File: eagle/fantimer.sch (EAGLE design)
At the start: 16 parts, among them IC1 PIC10F200, K1 PB2032-ND, Q1 2N7000-G, U1 IRM-01-5, X1 732-10957-ND

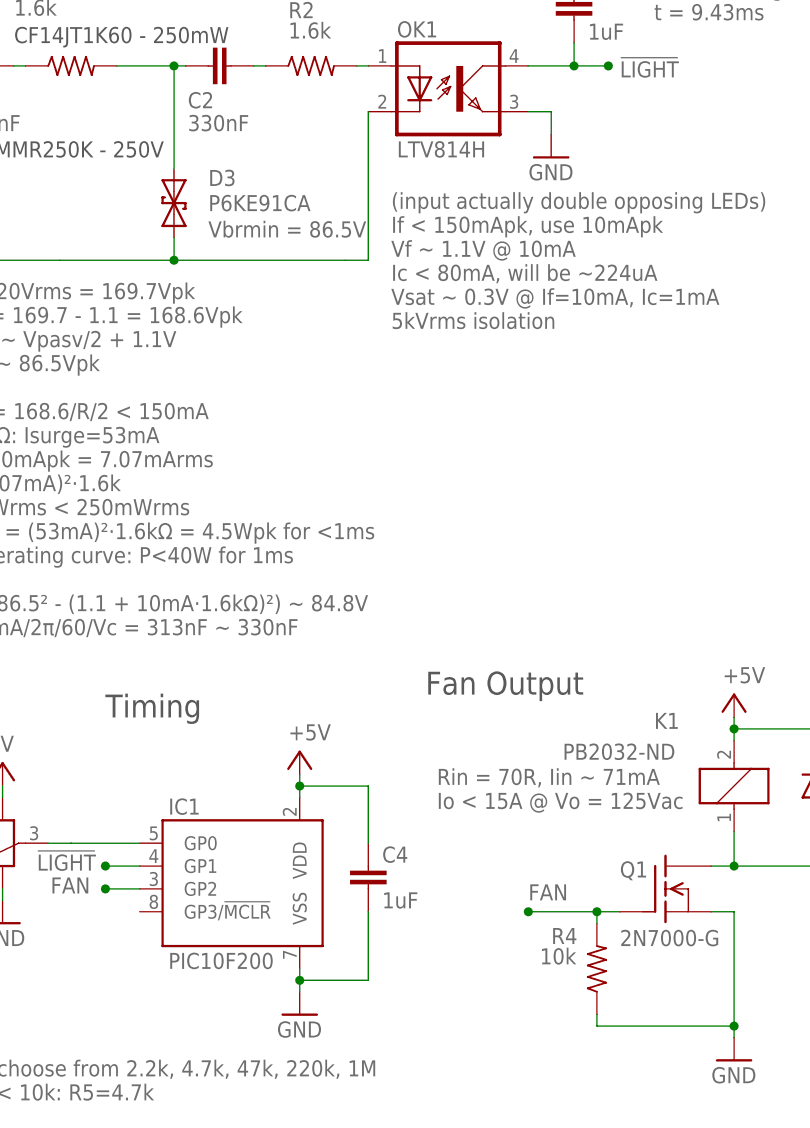
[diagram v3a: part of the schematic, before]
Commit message: Pulldown 100k. Fix up diodes, resistors and filter cap in BOM.
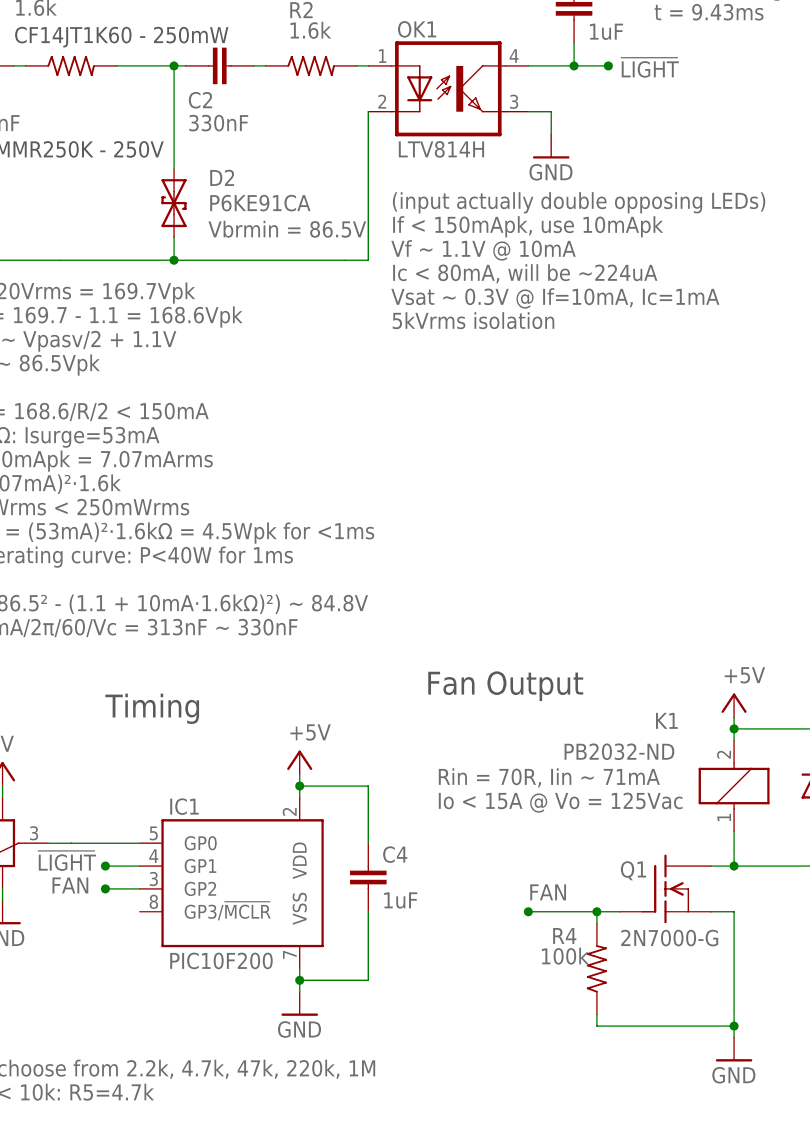
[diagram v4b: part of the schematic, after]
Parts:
- R4: value 10k -> 100k
- renumbered D3 to D2
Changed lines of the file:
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@@
 <part name="P+4" library="supply1" library_urn="urn:adsk.eagle:library:371" deviceset="+5V" device=""/>
 <part name="GND4" library="supply1" library_urn="urn:adsk.eagle:library:371" deviceset="GND" device=""/>
-<part name="D3" library="diode" library_urn="urn:adsk.eagle:library:210" deviceset="P6KEXXC" device="" package3d_urn="urn:adsk.eagle:package:43349/1" value="P6KE91CA"/>
+<part name="D2" library="diode" library_urn="urn:adsk.eagle:library:210" deviceset="P6KEXXC" device="" package3d_urn="urn:adsk.eagle:package:43349/1" value="P6KE91CA"/>
 <part name="C1" library="rcl" library_urn="urn:adsk.eagle:library:334" deviceset="C-EU" device="102-064X133" package3d_urn="urn:adsk.eagle:package:23653/1" value="330nF"/>
 <part name="C2" library="rcl" library_urn="urn:adsk.eagle:library:334" deviceset="C-EU" device="102-064X133" package3d_urn="urn:adsk.eagle:package:23653/1" value="330nF"/>
@@
 <part name="IC1" library="microchip-addl" deviceset="PIC10F220" device="-I/P" package3d_urn="urn:adsk.eagle:package:14440/1" value="PIC10F200"/>
 <part name="GND2" library="supply1" library_urn="urn:adsk.eagle:library:371" deviceset="GND" device=""/>
-<part name="R4" library="resistor" library_urn="urn:adsk.eagle:library:348" deviceset="R-US_" device="0207/7" package3d_urn="urn:adsk.eagle:package:25942/1" value="10k"/>
+<part name="R4" library="resistor" library_urn="urn:adsk.eagle:library:348" deviceset="R-US_" device="0207/7" package3d_urn="urn:adsk.eagle:package:25942/1" value="100k"/>
 <part name="C4" library="rcl" library_urn="urn:adsk.eagle:library:334" deviceset="C-EU" device="025-025X050" package3d_urn="urn:adsk.eagle:package:23629/2" value="1uF"/>
 </parts>
@@
 </instance>
 <instance part="GND4" gate="1" x="77.47" y="121.92"/>
-<instance part="D3" gate="1" x="35.56" y="115.57" smashed="yes" rot="R90">
+<instance part="D2" gate="1" x="35.56" y="115.57" smashed="yes" rot="R90">
 <attribute name="NAME" x="39.37" y="118.745" size="1.778" layer="95"/>
 <attribute name="VALUE" x="39.37" y="115.951" size="1.778" layer="96"/>
@@
 <pinref part="OK1" gate="G$1" pin="C"/>
 <wire x1="57.15" y1="125.73" x2="57.15" y2="127" width="0.1524" layer="91"/>
-<pinref part="D3" gate="1" pin="1"/>
+<pinref part="D2" gate="1" pin="1"/>
 <wire x1="35.56" y1="113.03" x2="35.56" y2="110.49" width="0.1524" layer="91"/>
 <junction x="35.56" y="110.49"/>
@@
 <net name="VZ" class="0">
 <segment>
-<pinref part="D3" gate="1" pin="2"/>
+<pinref part="D2" gate="1" pin="2"/>
 <wire x1="35.56" y1="120.65" x2="35.56" y2="132.08" width="0.1524" layer="91"/>
 <pinref part="C2" gate="G$1" pin="1"/>

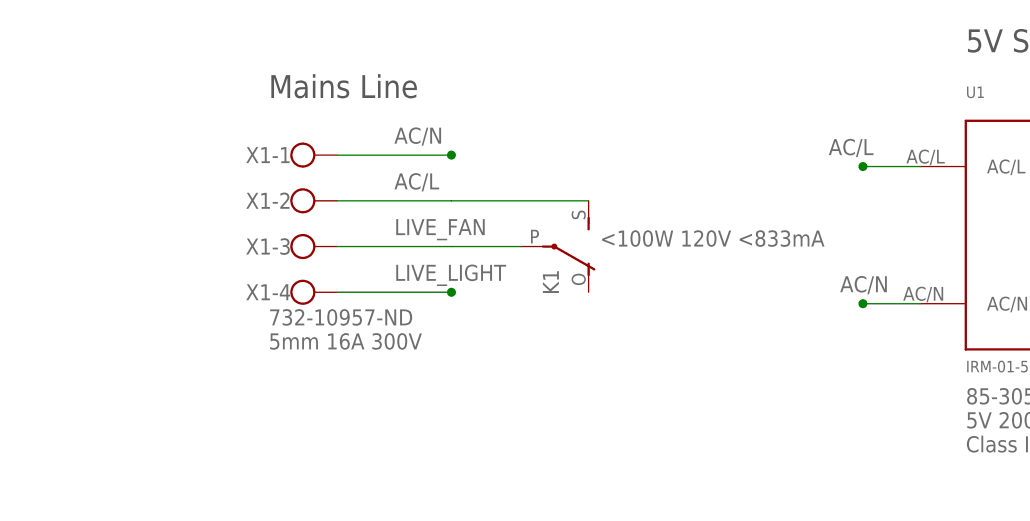
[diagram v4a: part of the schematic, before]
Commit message: Replace TVS with varistor across relay
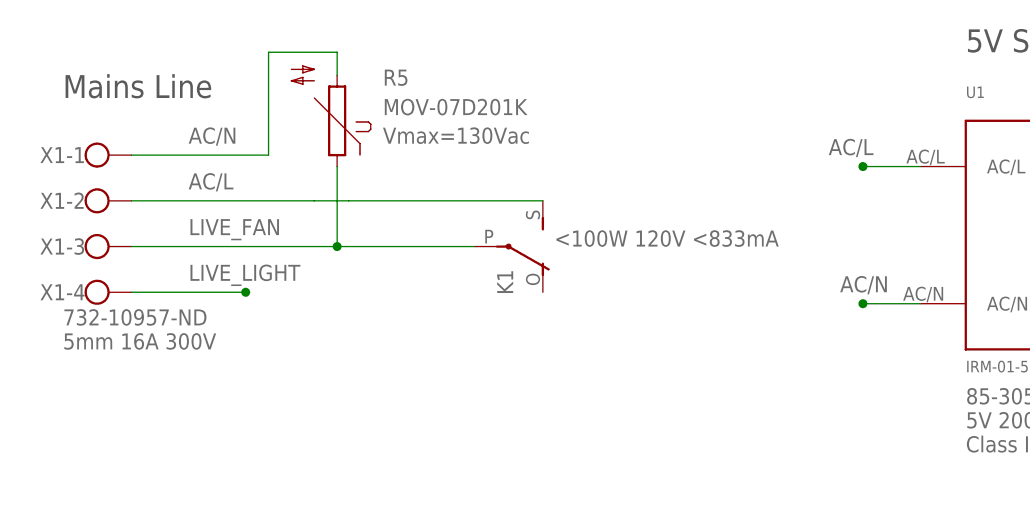
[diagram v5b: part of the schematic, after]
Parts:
- added R5: MOV-07D201K, varistor:S05K300
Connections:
- net AC/N: now also R5.2
- net LIVE_FAN: now also R5.1
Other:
- note added: "Vmax=130Vac"
- moved on the sheet: K1, X1-1, X1-2, X1-3, X1-4
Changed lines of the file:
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@@
 <part name="R4" library="resistor" library_urn="urn:adsk.eagle:library:348" deviceset="R-US_" device="0207/7" package3d_urn="urn:adsk.eagle:package:25942/1" value="100k"/>
 <part name="C4" library="rcl" library_urn="urn:adsk.eagle:library:334" deviceset="C-EU" device="025-025X050" package3d_urn="urn:adsk.eagle:package:23629/2" value="1uF"/>
+<part name="R5" library="varistor" library_urn="urn:adsk.eagle:library:410" deviceset="S05K300" device="" package3d_urn="urn:adsk.eagle:package:30536/1" value="MOV-07D201K"/>
 </parts>
 <sheets>
 <sheet>
 <plain>
-<text x="8.89" y="172.72" size="1.778" layer="96">5mm 16A 300V</text>
+<text x="-13.97" y="172.72" size="1.778" layer="96">5mm 16A 300V</text>
 <text x="7.62" y="21.59" size="1.778" layer="96" rot="MR180">R3 can choose from 2.2k, 4.7k, 47k, 220k, 1M
 Rinadc &lt; 10k: R5=4.7k</text>
@@
 5V 200mA out
 Class II isolation</text>
-<text x="45.72" y="184.15" size="1.778" layer="96">&lt;100W 120V &lt;833mA</text>
+<text x="40.64" y="184.15" size="1.778" layer="96">&lt;100W 120V &lt;833mA</text>
 <text x="64.77" y="49.53" size="1.778" layer="96">Rin = 70R, Iin ~ 71mA
 Io &lt; 15A @ Vo = 125Vac</text>
@@
 <text x="17.78" y="134.62" size="1.778" layer="97">CF14JT1K60‎ - 250mW</text>
 <text x="11.43" y="121.92" size="1.778" layer="97">334MMR250K‎ - 250V</text>
-<text x="8.89" y="200.66" size="2.54" layer="97">Mains Line</text>
+<text x="-13.97" y="200.66" size="2.54" layer="97">Mains Line</text>
 <text x="86.36" y="205.74" size="2.54" layer="97">5V Supply</text>
 <text x="11.43" y="147.32" size="2.54" layer="97">Line Detection</text>
 <text x="63.5" y="62.23" size="2.54" layer="97">Fan Output</text>
 <text x="27.94" y="59.69" size="2.54" layer="97">Timing</text>
+<text x="21.59" y="195.58" size="1.778" layer="96">Vmax=130Vac</text>
 </plain>
 <instances>
-<instance part="X1" gate="-1" x="11.43" y="194.31"/>
-<instance part="X1" gate="-2" x="11.43" y="189.23"/>
-<instance part="X1" gate="-3" x="11.43" y="184.15"/>
-<instance part="X1" gate="-4" x="11.43" y="179.07"/>
+<instance part="X1" gate="-1" x="-11.43" y="194.31"/>
+<instance part="X1" gate="-2" x="-11.43" y="189.23"/>
+<instance part="X1" gate="-3" x="-11.43" y="184.15"/>
+<instance part="X1" gate="-4" x="-11.43" y="179.07"/>
 <instance part="P+1" gate="1" x="120.65" y="200.66" smashed="yes">
 <attribute name="VALUE" x="119.38" y="201.93" size="1.778" layer="96"/>
@@
 <attribute name="PART" x="88.9" y="58.42" size="1.778" layer="95"/>
 </instance>
-<instance part="K1" gate="2" x="39.37" y="184.15" rot="R270"/>
+<instance part="K1" gate="2" x="34.29" y="184.15" rot="R270"/>
 <instance part="P+3" gate="1" x="97.79" y="62.23" smashed="yes">
 <attribute name="VALUE" x="96.52" y="63.5" size="1.778" layer="96"/>
@@
 </instance>
 <instance part="C4" gate="G$1" x="57.15" y="43.18"/>
+<instance part="R5" gate="G$1" x="16.51" y="198.12" smashed="yes" rot="R90">
+<attribute name="NAME" x="21.59" y="202.0316" size="1.778" layer="95"/>
+<attribute name="VALUE" x="21.59" y="198.755" size="1.778" layer="96"/>
+</instance>
 </instances>
 <busses>
@@
 <segment>
 <pinref part="X1" gate="-1" pin="KL"/>
-<wire x1="16.51" y1="194.31" x2="29.21" y2="194.31" width="0.1524" layer="91"/>
-<junction x="29.21" y="194.31"/>
-<label x="22.86" y="195.58" size="1.778" layer="95"/>
+<wire x1="-6.35" y1="194.31" x2="8.89" y2="194.31" width="0.1524" layer="91"/>
+<label x="0" y="195.58" size="1.778" layer="95"/>
+<wire x1="16.51" y1="203.2" x2="16.51" y2="205.74" width="0.1524" layer="91"/>
+<wire x1="16.51" y1="205.74" x2="8.89" y2="205.74" width="0.1524" layer="91"/>
+<wire x1="8.89" y1="205.74" x2="8.89" y2="194.31" width="0.1524" layer="91"/>
+<pinref part="R5" gate="G$1" pin="2"/>
 </segment>
 <segment>
@@
 <segment>
 <pinref part="X1" gate="-2" pin="KL"/>
-<wire x1="16.51" y1="189.23" x2="29.21" y2="189.23" width="0.1524" layer="91"/>
-<label x="22.86" y="190.5" size="1.778" layer="95"/>
+<wire x1="-6.35" y1="189.23" x2="13.97" y2="189.23" width="0.1524" layer="91"/>
+<wire x1="13.97" y1="189.23" x2="16.51" y2="189.23" width="0.1524" layer="91"/>
+<wire x1="16.51" y1="189.23" x2="17.78" y2="189.23" width="0.1524" layer="91"/>
+<label x="0" y="190.5" size="1.778" layer="95"/>
 <pinref part="K1" gate="2" pin="S"/>
-<wire x1="29.21" y1="189.23" x2="44.45" y2="189.23" width="0.1524" layer="91"/>
+<wire x1="17.78" y1="189.23" x2="39.37" y2="189.23" width="0.1524" layer="91"/>
 </segment>
 <segment>
@@
 <segment>
 <pinref part="X1" gate="-3" pin="KL"/>
-<wire x1="16.51" y1="184.15" x2="29.21" y2="184.15" width="0.1524" layer="91"/>
-<label x="22.86" y="185.42" size="1.778" layer="95"/>
+<wire x1="-6.35" y1="184.15" x2="16.51" y2="184.15" width="0.1524" layer="91"/>
+<label x="0" y="185.42" size="1.778" layer="95"/>
 <pinref part="K1" gate="2" pin="P"/>
-<wire x1="29.21" y1="184.15" x2="36.83" y2="184.15" width="0.1524" layer="91"/>
+<wire x1="16.51" y1="184.15" x2="31.75" y2="184.15" width="0.1524" layer="91"/>
+<wire x1="16.51" y1="193.04" x2="16.51" y2="184.15" width="0.1524" layer="91"/>
+<junction x="16.51" y="184.15"/>
+<pinref part="R5" gate="G$1" pin="1"/>
 </segment>
 </net>
@@
 <segment>
 <pinref part="X1" gate="-4" pin="KL"/>
-<wire x1="16.51" y1="179.07" x2="29.21" y2="179.07" width="0.1524" layer="91"/>
-<junction x="29.21" y="179.07"/>
-<label x="22.86" y="180.34" size="1.778" layer="95"/>
+<wire x1="-6.35" y1="179.07" x2="6.35" y2="179.07" width="0.1524" layer="91"/>
+<junction x="6.35" y="179.07"/>
+<label x="0" y="180.34" size="1.778" layer="95"/>
 </segment>
 <segment>

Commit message: Library updates
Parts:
- IC1: value PIC10F200 -> PIC10F220
- U1: device meanwell:IRM-01 -> meanwell:IRM-01-5
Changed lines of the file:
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@@
 <part name="P+3" library="supply1" library_urn="urn:adsk.eagle:library:371" deviceset="+5V" device=""/>
 <part name="D1" library="diode" library_urn="urn:adsk.eagle:library:210" deviceset="DIODE-" device="DO41-7.6" package3d_urn="urn:adsk.eagle:package:43421/1" value="SB140TA"/>
-<part name="U1" library="meanwell" deviceset="IRM-01" device="" value="IRM-01-5"/>
+<part name="U1" library="meanwell" deviceset="IRM-01-5" device="" value="IRM-01-5"/>
 <part name="OK1" library="optocoupler" library_urn="urn:adsk.eagle:library:320" deviceset="LTV816" device="" package3d_urn="urn:adsk.eagle:package:21938/1" value="LTV814H"/>
-<part name="R2" library="resistor" library_urn="urn:adsk.eagle:library:348" deviceset="R-US_" device="0207/7" package3d_urn="urn:adsk.eagle:package:25942/1" value="1.6k"/>
+<part name="R2" library="resistor" library_urn="urn:adsk.eagle:library:348" deviceset="R-US_" device="0207/7" package3d_urn="urn:adsk.eagle:package:23493/1" value="1.6k"/>
 <part name="P+4" library="supply1" library_urn="urn:adsk.eagle:library:371" deviceset="+5V" device=""/>
 <part name="GND4" library="supply1" library_urn="urn:adsk.eagle:library:371" deviceset="GND" device=""/>
@@
 <part name="C1" library="rcl" library_urn="urn:adsk.eagle:library:334" deviceset="C-EU" device="102-064X133" package3d_urn="urn:adsk.eagle:package:23653/1" value="330nF"/>
 <part name="C2" library="rcl" library_urn="urn:adsk.eagle:library:334" deviceset="C-EU" device="102-064X133" package3d_urn="urn:adsk.eagle:package:23653/1" value="330nF"/>
-<part name="R1" library="resistor" library_urn="urn:adsk.eagle:library:348" deviceset="R-US_" device="0207/7" package3d_urn="urn:adsk.eagle:package:25942/1" value="1.6k"/>
+<part name="R1" library="resistor" library_urn="urn:adsk.eagle:library:348" deviceset="R-US_" device="0207/7" package3d_urn="urn:adsk.eagle:package:23493/1" value="1.6k"/>
 <part name="R3" library="rcl" library_urn="urn:adsk.eagle:library:334" deviceset="POTENTIOMETER_" device="PT-10" package3d_urn="urn:adsk.eagle:package:23786/1" value="4.7k"/>
 <part name="P+6" library="supply1" library_urn="urn:adsk.eagle:library:371" deviceset="+5V" device=""/>
@@
 <part name="C3" library="rcl" library_urn="urn:adsk.eagle:library:334" deviceset="C-EU" device="025-025X050" package3d_urn="urn:adsk.eagle:package:23629/2" value="1uF"/>
 <part name="P+2" library="supply1" library_urn="urn:adsk.eagle:library:371" deviceset="+5V" device=""/>
-<part name="IC1" library="microchip-addl" deviceset="PIC10F220" device="-I/P" package3d_urn="urn:adsk.eagle:package:14440/1" value="PIC10F200"/>
+<part name="IC1" library="microchip-addl" deviceset="PIC10F220" device="-I/P" package3d_urn="urn:adsk.eagle:package:14440/1" value="PIC10F220"/>
 <part name="GND2" library="supply1" library_urn="urn:adsk.eagle:library:371" deviceset="GND" device=""/>
-<part name="R4" library="resistor" library_urn="urn:adsk.eagle:library:348" deviceset="R-US_" device="0207/7" package3d_urn="urn:adsk.eagle:package:25942/1" value="100k"/>
+<part name="R4" library="resistor" library_urn="urn:adsk.eagle:library:348" deviceset="R-US_" device="0207/7" package3d_urn="urn:adsk.eagle:package:23493/1" value="100k"/>
 <part name="C4" library="rcl" library_urn="urn:adsk.eagle:library:334" deviceset="C-EU" device="025-025X050" package3d_urn="urn:adsk.eagle:package:23629/2" value="1uF"/>
 <part name="R5" library="varistor" library_urn="urn:adsk.eagle:library:410" deviceset="S05K300" device="" package3d_urn="urn:adsk.eagle:package:30536/1" value="MOV-07D201K"/>
@@
 <attribute name="VALUE" x="17.78" y="55.88" size="1.778" layer="96" rot="MR0"/>
 </instance>
-<instance part="IC1" gate="G$1" x="46.99" y="44.45"/>
+<instance part="IC1" gate="G$1" x="43.18" y="41.91"/>
 <instance part="GND2" gate="1" x="49.53" y="26.67"/>
 <instance part="R4" gate="G$1" x="82.55" y="31.75" smashed="yes" rot="R90">

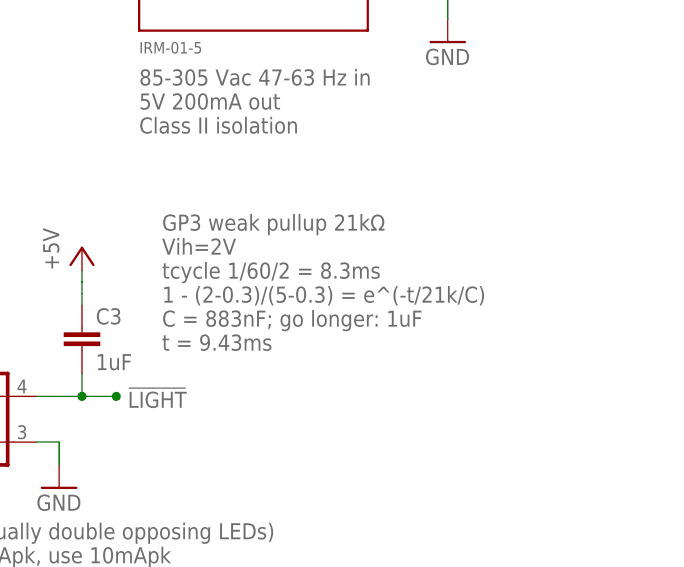
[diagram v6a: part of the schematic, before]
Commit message: Fix pullup info
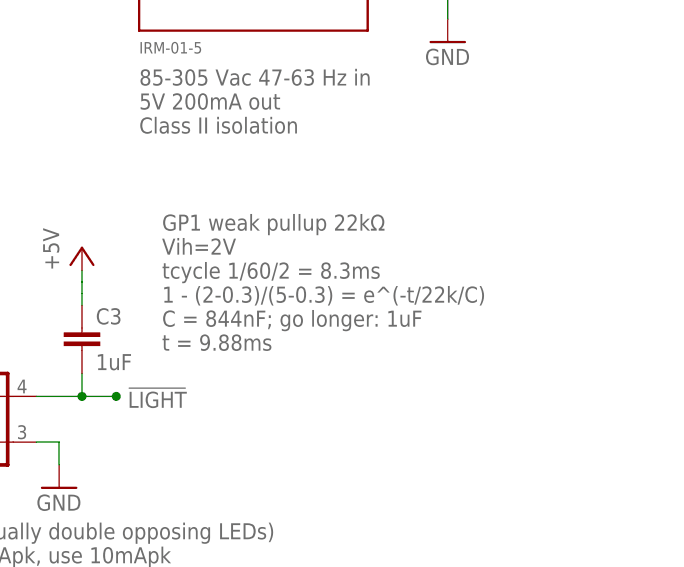
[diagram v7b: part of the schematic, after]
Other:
- note added: "GP1 weak pullup 22kΩ Vih=2V tcycle 1/60/2 = 8.3ms 1 - (2-0.3)/(5-0.3) = e^(-t/22k/C) C = 844nF; go longer: 1uF t = 9.88ms"
- note removed: "GP3 weak pullup 21kΩ Vih=2V tcycle 1/60/2 = 8.3ms 1 - (2-0.3)/(5-0.3) = e^(-t/21k/C) C = 883nF; go longer: 1uF t = 9.43ms"
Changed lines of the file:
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@@
 C = 10mA/2π/60/Vc = 313nF ~ 330nF</text>
 <text x="39.37" y="113.03" size="1.778" layer="96">Vbrmin = 86.5V</text>
-<text x="88.9" y="137.16" size="1.778" layer="96">GP3 weak pullup 21kΩ
+<text x="88.9" y="137.16" size="1.778" layer="96">GP1 weak pullup 22kΩ
 Vih=2V
 tcycle 1/60/2 = 8.3ms
-1 - (2-0.3)/(5-0.3) = e^(-t/21k/C)
-C = 883nF; go longer: 1uF
-t = 9.43ms</text>
+1 - (2-0.3)/(5-0.3) = e^(-t/22k/C)
+C = 844nF; go longer: 1uF
+t = 9.88ms</text>
 <text x="17.78" y="134.62" size="1.778" layer="97">CF14JT1K60‎ - 250mW</text>
 <text x="11.43" y="121.92" size="1.778" layer="97">334MMR250K‎ - 250V</text>
